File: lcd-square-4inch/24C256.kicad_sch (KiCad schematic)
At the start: 4 parts, among them U6 CAT24C256

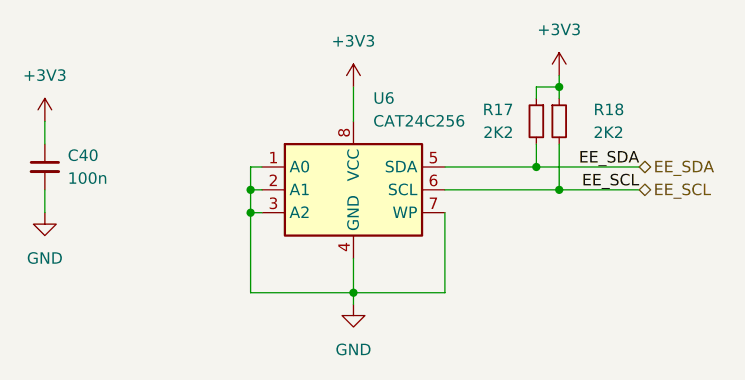
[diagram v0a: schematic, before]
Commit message: Add QSPI Flash trace length matching to 5 inch LCD
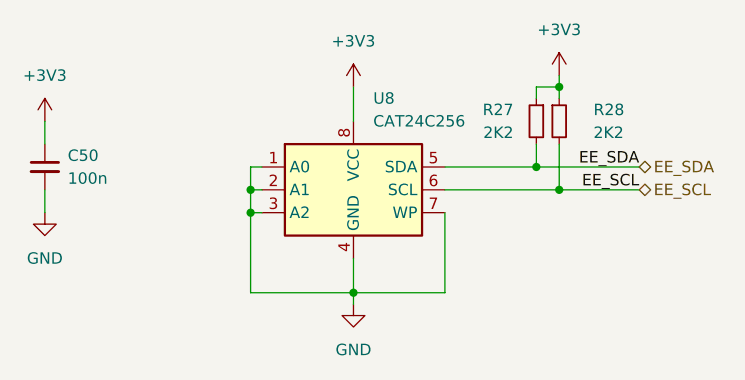
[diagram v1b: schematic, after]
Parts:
- renumbered C40 to C50, R17 to R27, R18 to R28, U6 to U8
